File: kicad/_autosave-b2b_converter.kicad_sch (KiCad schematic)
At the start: 0 parts

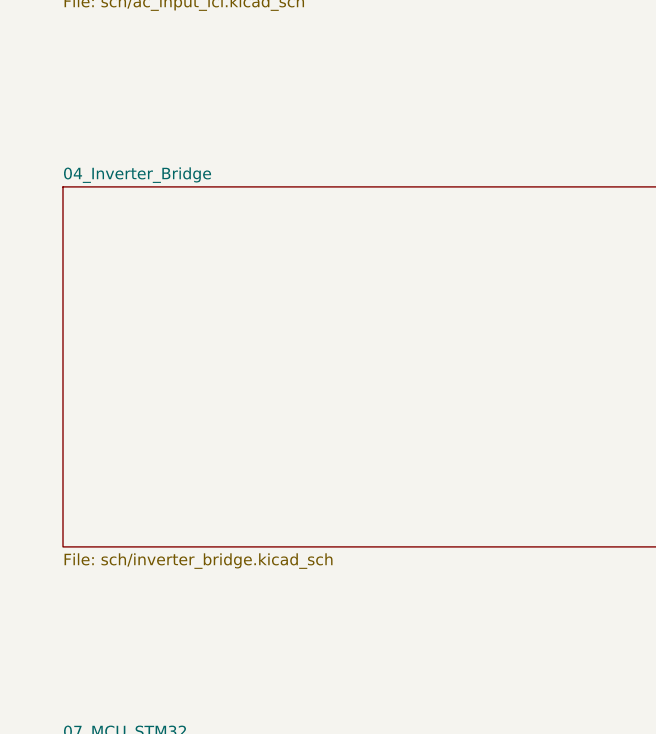
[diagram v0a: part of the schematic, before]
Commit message: Anade protecciones electricas y stackup con color
PROTECCIONES (de 15 a 56 componentes de proteccion, 272 en total)

  12x TVS gate-source, una por SiC. Sin ella un pico de dv/dt acoplado
      por Cgd puede perforar el oxido de puerta: es el modo de fallo mas
      comun en SiC. Va en el pie del transistor.
  12x snubber RC del nodo de conmutacion (220 pF + 4.7 ohm). El valor sale
      del barrido en LTspice: baja el dv/dt de 147 a 90 V/ns, por debajo
      del CMTI de 100 V/ns del UCC21520, y la sobretension de 823 a 767 V.
   2x TVS en serie sobre el bus DC (5KP440A): recorte en nanosegundos muy
      por delante del chopper, que es un lazo de control.
  12x Schottky de recorte en las entradas de ADC. La R serie del filtro
      anti-alias limita la corriente; sin los diodos, un transitorio de la
      etapa de potencia entra directo al pin del STM32.
   4x TVS de ESD en el conector de campo del ESP32.
   1x polyfuse rearmable + diodo antiinversion + TVS en la entrada de 24 V.

BUGS DESTAPADOS AL CABLEAR LAS PROTECCIONES

  a) Los 4 TVS del conector de campo compartian columna: sus bajadas a
     IOGND se solapaban y cortocircuitaban las cuatro lineas. Cada uno a
     su propia x.
  b) Los diodos de recorte del ADC morian en MITAD del cable de senal, asi
     que KiCad no los conectaba (solo une extremo con extremo, el mismo
     fallo que ya aparecio en los rieles del bus). El cable se parte ahora
     en el punto de recorte.

ASPECTO

  El .kicad_pcb no tenia seccion (stackup), por eso el render salia verde
  por defecto. Se inyecta desde tools/stackup_tpl.txt: mascara negra,
  serigrafia blanca, acabado ENIG (obligado con el LQFP-100 de paso
  0.5 mm) y los espesores reales de cobre (70 um exteriores, 35 um
  interiores) con prepreg fino de 0.2 mm entre F.Cu e In1.Cu para que el
  bus laminado tenga poca inductancia. Los colores son parametros al
  principio de tools/gen_pcb.py.

Co-Authored-By: Claude Opus 5 <noreply@anthropic.com>
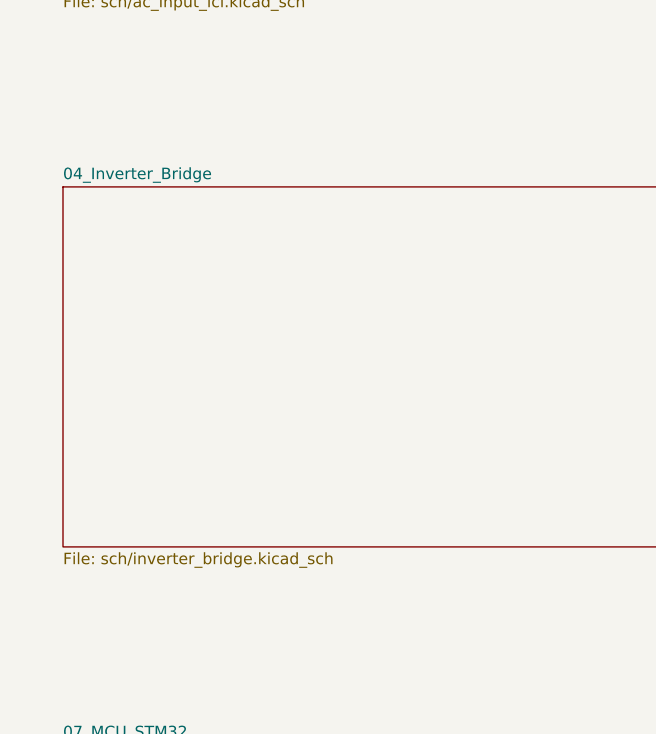
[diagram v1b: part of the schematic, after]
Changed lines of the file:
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@@
 (kicad_sch
 	(version 20250114)
-	(generator "kisch.py")
+	(generator "eeschema")
 	(generator_version "9.0")
 	(paper "A2")
@@
 		(at 30 70)
 		(size 150 40)
-		(fields_autoplaced yes)
-		(stroke
-			(width 0.1524)
-			(type solid)
-		)
-		(fill
-			(color 0 0 0 0)
+		(exclude_from_sim no)
+		(in_bom yes)
+		(on_board yes)
+		(dnp no)
+		(fields_autoplaced yes)
+		(stroke
+			(width 0.1524)
+			(type solid)
+		)
+		(fill
+			(color 0 0 0 0.0000)
 		)
 		(property "Sheetname" "01_AC_Input_LCL"
@@
 		(at 205 70)
 		(size 150 40)
-		(fields_autoplaced yes)
-		(stroke
-			(width 0.1524)
-			(type solid)
-		)
-		(fill
-			(color 0 0 0 0)
+		(exclude_from_sim no)
+		(in_bom yes)
+		(on_board yes)
+		(dnp no)
+		(fields_autoplaced yes)
+		(stroke
+			(width 0.1524)
+			(type solid)
+		)
+		(fill
+			(color 0 0 0 0.0000)
 		)
 		(property "Sheetname" "02_AFE_Bridge"
@@
 		(at 380 70)
 		(size 150 40)
-		(fields_autoplaced yes)
-		(stroke
-			(width 0.1524)
-			(type solid)
-		)
-		(fill
-			(color 0 0 0 0)
+		(exclude_from_sim no)
+		(in_bom yes)
+		(on_board yes)
+		(dnp no)
+		(fields_autoplaced yes)
+		(stroke
+			(width 0.1524)
+			(type solid)
+		)
+		(fill
+			(color 0 0 0 0.0000)
 		)
 		(property "Sheetname" "03_DClink_Precharge"
@@
 		(at 30 132)
 		(size 150 40)
-		(fields_autoplaced yes)
-		(stroke
-			(width 0.1524)
-			(type solid)
-		)
-		(fill
-			(color 0 0 0 0)
+		(exclude_from_sim no)
+		(in_bom yes)
+		(on_board yes)
+		(dnp no)
+		(fields_autoplaced yes)
+		(stroke
+			(width 0.1524)
+			(type solid)
+		)
+		(fill
+			(color 0 0 0 0.0000)
 		)
 		(property "Sheetname" "04_Inverter_Bridge"
-			(at 30 131.3 0)
+			(at 30 131.2884 0)
 			(effects
 				(font
@@
 		)
 		(property "Sheetfile" "sch/inverter_bridge.kicad_sch"
-			(at 30 172.7 0)
+			(at 30 172.5846 0)
 			(effects
 				(font
@@
 		(at 205 132)
 		(size 150 40)
-		(fields_autoplaced yes)
-		(stroke
-			(width 0.1524)
-			(type solid)
-		)
-		(fill
-			(color 0 0 0 0)
+		(exclude_from_sim no)
+		(in_bom yes)
+		(on_board yes)
+		(dnp no)
+		(fields_autoplaced yes)
+		(stroke
+			(width 0.1524)
+			(type solid)
+		)
+		(fill
+			(color 0 0 0 0.0000)
 		)
 		(property "Sheetname" "05_Gate_Drivers"
@@
 		(at 380 132)
 		(size 150 40)
-		(fields_autoplaced yes)
-		(stroke
-			(width 0.1524)
-			(type solid)
-		)
-		(fill
-			(color 0 0 0 0)
+		(exclude_from_sim no)
+		(in_bom yes)
+		(on_board yes)
+		(dnp no)
+		(fields_autoplaced yes)
+		(stroke
+			(width 0.1524)
+			(type solid)
+		)
+		(fill
+			(color 0 0 0 0.0000)
 		)
 		(property "Sheetname" "06_Sense_I_V"
@@
 		(at 30 194)
 		(size 150 40)
-		(fields_autoplaced yes)
-		(stroke
-			(width 0.1524)
-			(type solid)
-		)
-		(fill
-			(color 0 0 0 0)
+		(exclude_from_sim no)
+		(in_bom yes)
+		(on_board yes)
+		(dnp no)
+		(fields_autoplaced yes)
+		(stroke
+			(width 0.1524)
+			(type solid)
+		)
+		(fill
+			(color 0 0 0 0.0000)
 		)
 		(property "Sheetname" "07_MCU_STM32"
@@
 		(at 205 194)
 		(size 150 40)
-		(fields_autoplaced yes)
-		(stroke
-			(width 0.1524)
-			(type solid)
-		)
-		(fill
-			(color 0 0 0 0)
+		(exclude_from_sim no)
+		(in_bom yes)
+		(on_board yes)
+		(dnp no)
+		(fields_autoplaced yes)
+		(stroke
+			(width 0.1524)
+			(type solid)
+		)
+		(fill
+			(color 0 0 0 0.0000)
 		)
 		(property "Sheetname" "08_Protection_IO"
@@
 		(at 380 194)
 		(size 150 40)
-		(fields_autoplaced yes)
-		(stroke
-			(width 0.1524)
-			(type solid)
-		)
-		(fill
-			(color 0 0 0 0)
+		(exclude_from_sim no)
+		(in_bom yes)
+		(on_board yes)
+		(dnp no)
+		(fields_autoplaced yes)
+		(stroke
+			(width 0.1524)
+			(type solid)
+		)
+		(fill
+			(color 0 0 0 0.0000)
 		)
 		(property "Sheetname" "09_PSU_Aux_Bias"
@@
 		(at 30 256)
 		(size 150 40)
-		(fields_autoplaced yes)
-		(stroke
-			(width 0.1524)
-			(type solid)
-		)
-		(fill
-			(color 0 0 0 0)
+		(exclude_from_sim no)
+		(in_bom yes)
+		(on_board yes)
+		(dnp no)
+		(fields_autoplaced yes)
+		(stroke
+			(width 0.1524)
+			(type solid)
+		)
+		(fill
+			(color 0 0 0 0.0000)
 		)
 		(property "Sheetname" "10_Isolation_Comms"
@@
 		(at 205 256)
 		(size 150 40)
-		(fields_autoplaced yes)
-		(stroke
-			(width 0.1524)
-			(type solid)
-		)
-		(fill
-			(color 0 0 0 0)
+		(exclude_from_sim no)
+		(in_bom yes)
+		(on_board yes)
+		(dnp no)
+		(fields_autoplaced yes)
+		(stroke
+			(width 0.1524)
+			(type solid)
+		)
+		(fill
+			(color 0 0 0 0.0000)
 		)
 		(property "Sheetname" "11_ESP32_IoT"
